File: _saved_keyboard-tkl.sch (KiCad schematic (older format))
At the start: 116 parts, among them P1 USB_OTG, P2 JTAG, SW1 MX, SW2 MX, SW3 MX, SW4 MX, SW5 MX, SW6 MX, SW7 MX, SW8 MX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

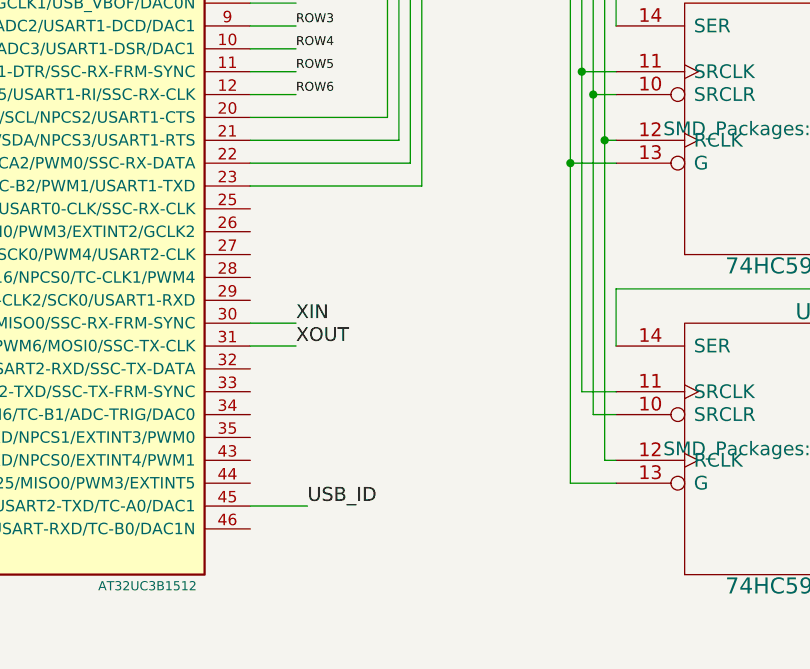
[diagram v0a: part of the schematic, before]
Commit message: Added status LEDs but they can't be driven by the micro.
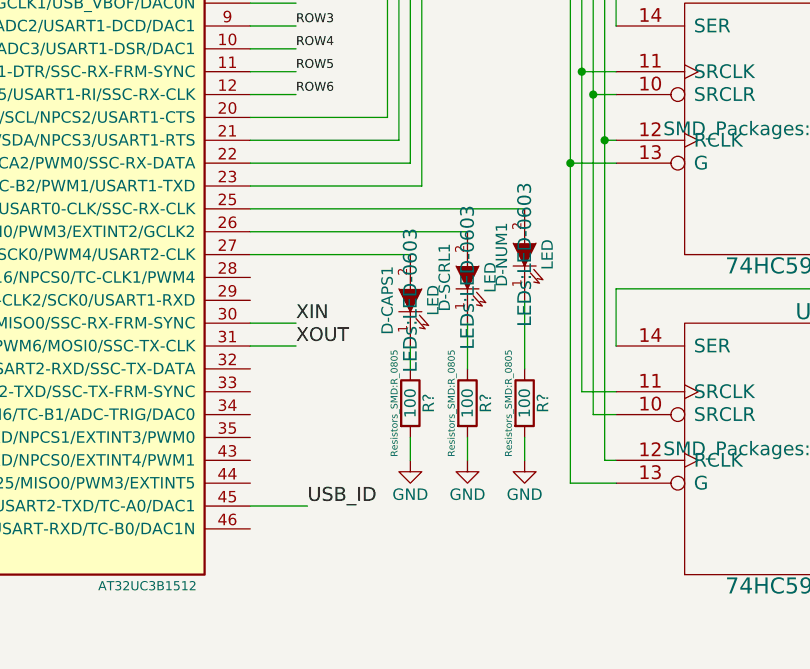
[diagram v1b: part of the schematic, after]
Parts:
- added D-CAPS1, D-NUM1, D-SCRL1: LED, LEDs:LED-0603, symbol LED
- added R? (x3): 100, Resistors_SMD:R_0805, symbol R
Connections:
- net GND: now also R?.2, R?.2, R?.2
- net at U1.25 (PA13/GPIO13/NMI/PWM2/USART0-CLK/SSC-RX-CLK): now also D-NUM1.2 (A)
- net at U1.26 (PA14/GPIO1/MOSI0/PWM3/EXTINT2/GCLK2): now also D-SCRL1.2 (A)
- net at U1.27 (PA15/GPIO15/SCK0/PWM4/USART2-CLK): now also D-CAPS1.2 (A)
- new net: D-NUM1.1 (K), R?.1
- new net: D-SCRL1.1 (K), R?.1
- new net: D-CAPS1.1 (K), R?.1
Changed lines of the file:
@@
 	1    0    0    -1
 $EndComp
+$Comp
+L LED D-NUM1
+U 1 1 55E29E33
+P 6250 6550
+F 0 "D-NUM1" H 6250 6650 50  0000 C CNN
+F 1 "LED" H 6250 6450 50  0000 C CNN
+F 2 "LEDs:LED-0603" H 6250 6550 60  0000 C CNN
+F 3 "" H 6250 6550 60  0000 C CNN
+F 4 "630-ASMT-CW00" H 6250 6550 60  0001 C CNN "Mouser Part #"
+	1    6250 6550
+	0    -1   -1   0
+$EndComp
+$Comp
+L LED D-SCRL1
+U 1 1 55E2A000
+P 6000 6650
+F 0 "D-SCRL1" H 6000 6750 50  0000 C CNN
+F 1 "LED" H 6000 6550 50  0000 C CNN
+F 2 "LEDs:LED-0603" H 6000 6650 60  0000 C CNN
+F 3 "" H 6000 6650 60  0000 C CNN
+F 4 "630-ASMT-CW00" H 6000 6650 60  0001 C CNN "Mouser Part #"
+	1    6000 6650
+	0    -1   -1   0
+$EndComp
+$Comp
+L LED D-CAPS1
+U 1 1 55E2A180
+P 5750 6750
+F 0 "D-CAPS1" H 5750 6850 50  0000 C CNN
+F 1 "LED" H 5750 6650 50  0000 C CNN
+F 2 "LEDs:LED-0603" H 5750 6750 60  0000 C CNN
+F 3 "" H 5750 6750 60  0000 C CNN
+F 4 "630-ASMT-CW00" H 5750 6750 60  0001 C CNN "Mouser Part #"
+	1    5750 6750
+	0    -1   -1   0
+$EndComp
+Wire Wire Line
+	5050 6350 6250 6350
+Wire Wire Line
+	5050 6450 6000 6450
+Wire Wire Line
+	5050 6550 5750 6550
+$Comp
+L GND #PWR?
+U 1 1 55E2B688
+P 5750 7450
+F 0 "#PWR?" H 5750 7200 50  0001 C CNN
+F 1 "GND" H 5750 7300 50  0000 C CNN
+F 2 "" H 5750 7450 60  0000 C CNN
+F 3 "" H 5750 7450 60  0000 C CNN
+	1    5750 7450
+	1    0    0    -1
+$EndComp
+$Comp
+L GND #PWR?
+U 1 1 55E2CFAD
+P 6000 7450
+F 0 "#PWR?" H 6000 7200 50  0001 C CNN
+F 1 "GND" H 6000 7300 50  0000 C CNN
+F 2 "" H 6000 7450 60  0000 C CNN
+F 3 "" H 6000 7450 60  0000 C CNN
+	1    6000 7450
+	1    0    0    -1
+$EndComp
+$Comp
+L GND #PWR?
+U 1 1 55E2D11D
+P 6250 7450
+F 0 "#PWR?" H 6250 7200 50  0001 C CNN
+F 1 "GND" H 6250 7300 50  0000 C CNN
+F 2 "" H 6250 7450 60  0000 C CNN
+F 3 "" H 6250 7450 60  0000 C CNN
+	1    6250 7450
+	1    0    0    -1
+$EndComp
+$Comp
+L R R?
+U 1 1 55E2D3F4
+P 5750 7200
+F 0 "R?" V 5830 7200 50  0000 C CNN
+F 1 "100" V 5750 7200 50  0000 C CNN
+F 2 "Resistors_SMD:R_0805" V 5680 7200 30  0000 C CNN
+F 3 "" H 5750 7200 30  0000 C CNN
+	1    5750 7200
+	1    0    0    -1
+$EndComp
+$Comp
+L R R?
+U 1 1 55E2D57D
+P 6000 7200
+F 0 "R?" V 6080 7200 50  0000 C CNN
+F 1 "100" V 6000 7200 50  0000 C CNN
+F 2 "Resistors_SMD:R_0805" V 5930 7200 30  0000 C CNN
+F 3 "" H 6000 7200 30  0000 C CNN
+	1    6000 7200
+	1    0    0    -1
+$EndComp
+$Comp
+L R R?
+U 1 1 55E2D6FC
+P 6250 7200
+F 0 "R?" V 6330 7200 50  0000 C CNN
+F 1 "100" V 6250 7200 50  0000 C CNN
+F 2 "Resistors_SMD:R_0805" V 6180 7200 30  0000 C CNN
+F 3 "" H 6250 7200 30  0000 C CNN
+	1    6250 7200
+	1    0    0    -1
+$EndComp
+Wire Wire Line
+	5750 7350 5750 7450
+Wire Wire Line
+	6000 7350 6000 7450
+Wire Wire Line
+	6250 7350 6250 7450
+Wire Wire Line
+	6250 6750 6250 7050
+Wire Wire Line
+	6000 6850 6000 7050
+Wire Wire Line
+	5750 6950 5750 7050
 $EndSCHEMATC
